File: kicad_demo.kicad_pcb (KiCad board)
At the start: 2 copper layers, 100 x 50 mm, 19 parts, among them P1 pwr, P2 key, Q1 2N3053, Y1 7020 kHz

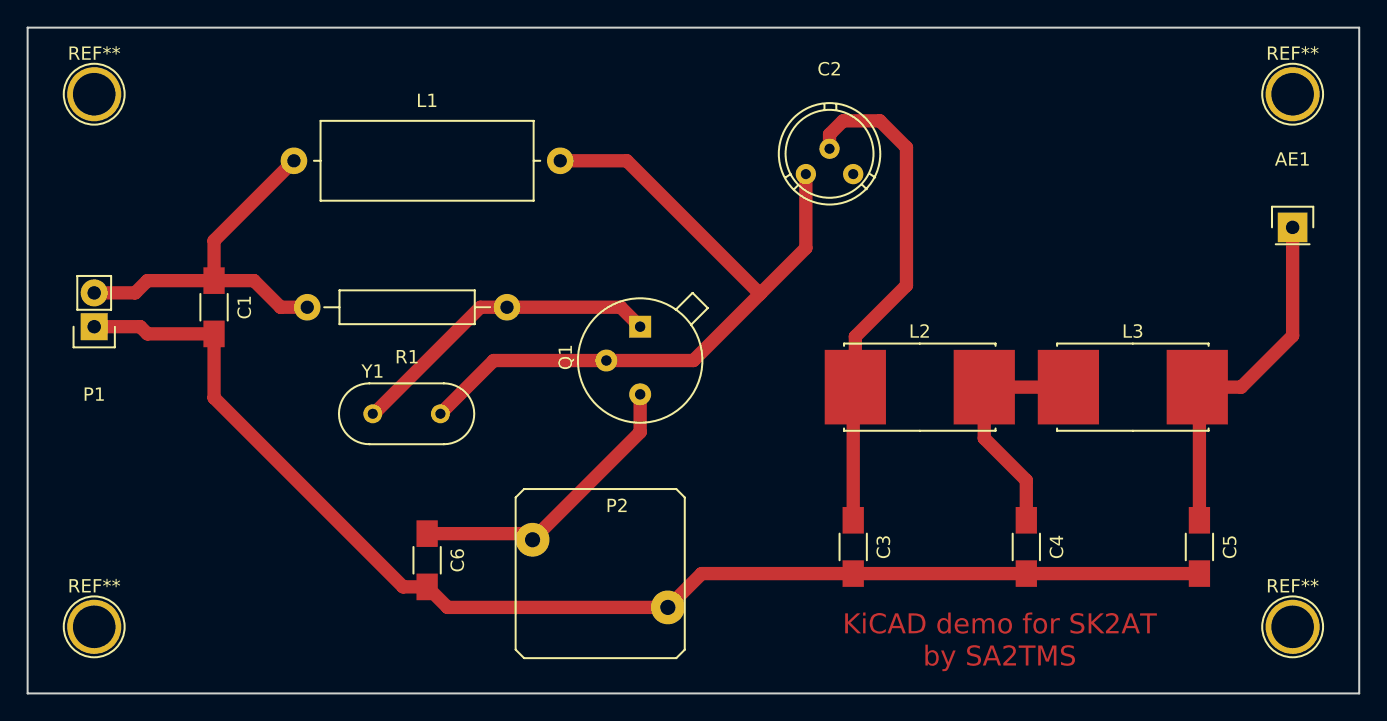
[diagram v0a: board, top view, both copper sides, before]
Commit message: Rough layout
Want to route signal and GND on top to minimize current loop size
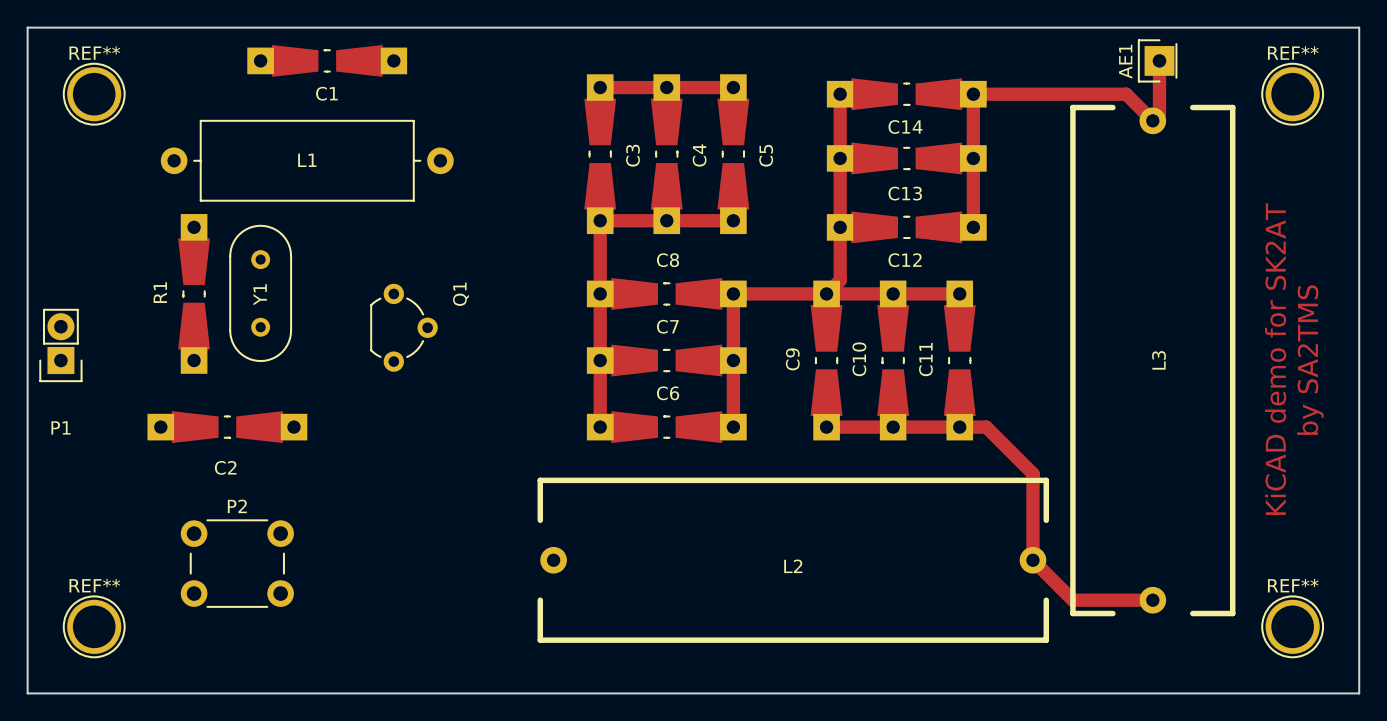
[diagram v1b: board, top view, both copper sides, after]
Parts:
- added C10: 60p, Resistors_Universal:Resistor_SMD+THTuniversal_0805to1206_RM10_HandSoldering, F.Cu at (115.0, 100.0)
- added C11: 5p, Resistors_Universal:Resistor_SMD+THTuniversal_0805to1206_RM10_HandSoldering, F.Cu at (120.0, 100.0)
- added C12: 200p, Resistors_Universal:Resistor_SMD+THTuniversal_0805to1206_RM10_HandSoldering, F.Cu at (116.0, 90.0)
- added C13: 60p, Resistors_Universal:Resistor_SMD+THTuniversal_0805to1206_RM10_HandSoldering, F.Cu at (116.0, 84.8)
- added C14: 7p, Resistors_Universal:Resistor_SMD+THTuniversal_0805to1206_RM10_HandSoldering, F.Cu at (116.0, 80.0)
- added C7: 60p, Resistors_Universal:Resistor_SMD+THTuniversal_0805to1206_RM10_HandSoldering, F.Cu at (98.0, 100.0)
- added C8: 7p, Resistors_Universal:Resistor_SMD+THTuniversal_0805to1206_RM10_HandSoldering, F.Cu at (98.0, 95.0)
- added C9: 800p, Resistors_Universal:Resistor_SMD+THTuniversal_0805to1206_RM10_HandSoldering, F.Cu at (110.0, 100.0)
- AE1: value Antenna -> Ant
- C1: footprint Capacitors_SMD:C_1206_HandSoldering -> Resistors_Universal:Resistor_SMD+THTuniversal_0805to1206_RM10_HandSoldering
- C2: value 1000pF -> 10nF; footprint Potentiometers:Potentiometer_Bourns_3339H_Angular_ScrewUp -> Resistors_Universal:Resistor_SMD+THTuniversal_0805to1206_RM10_HandSoldering
- C3, C5: value 267pF -> 100p; footprint Capacitors_SMD:C_1206_HandSoldering -> Resistors_Universal:Resistor_SMD+THTuniversal_0805to1206_RM10_HandSoldering
- C4: value 865pF -> 100p; footprint Capacitors_SMD:C_1206_HandSoldering -> Resistors_Universal:Resistor_SMD+THTuniversal_0805to1206_RM10_HandSoldering
- C6: value 10nF -> 200p; footprint Capacitors_SMD:C_1206_HandSoldering -> Resistors_Universal:Resistor_SMD+THTuniversal_0805to1206_RM10_HandSoldering
- L2, L3: footprint Inductors:Inductor_Vishay_IHSM-3825 -> PROJECT:1u75_coil
- P2: footprint Buttons_Switches_ThroughHole:SW_PUSH -> Buttons_Switches_ThroughHole:SW_PUSH_6mm
- Q1: value 2N3053 -> BC546; footprint TO_SOT_Packages_THT:TO39EBC -> TO_SOT_Packages_THT:TO-92_Molded_Wide
- R1: footprint Resistors_ThroughHole:Resistor_Horizontal_RM15mm -> Resistors_Universal:Resistor_SMD+THTuniversal_0805to1206_RM10_HandSoldering
- moved C2 47.4 mm to (65.0, 105.0), turned to 180 degrees
- moved C5 45.8 mm to (103.0, 84.5)
- moved C4 40.0 mm to (98.0, 84.5)
- moved C3 35.1 mm to (93.0, 84.5)
- moved P2 30.6 mm to (62.5, 113.0)
- moved R1 23.5 mm to (62.5, 95.0), turned to 90 degrees
- moved C6 20.6 mm to (98.0, 105.0), turned to 0 degrees
- moved C1 20.4 mm to (72.5, 77.5), turned to 0 degrees
- moved Q1 18.7 mm to (77.5, 95.0)
- moved L2 16.1 mm to (107.5, 115.0)
- moved AE1 16.0 mm to (135.0, 77.5), turned to 90 degrees
- moved Y1 10.6 mm to (67.5, 97.5), turned to 90 degrees
- moved L1 9.00 mm to (71.0, 85.0)
- moved P1 3.56 mm to (52.5, 100.0)
- moved L3 2.50 mm to (134.5, 100.0), turned to 90 degrees
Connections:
- C2 pad 2: Net-(C2-Pad2) -> GND
- C3 pad 1: Net-(C2-Pad2) -> Net-(C3-Pad1)
- C3 pad 2: GND -> Net-(C3-Pad2)
- C4 pad 1: Net-(C4-Pad1) -> Net-(C3-Pad1)
- C4 pad 2: GND -> Net-(C3-Pad2)
- C5 pad 1: Net-(AE1-Pad1) -> Net-(C3-Pad1)
- C5 pad 2: GND -> Net-(C3-Pad2)
- C6 pad 1: Net-(C6-Pad1) -> Net-(C3-Pad2)
- L1 pad 2: Net-(C2-Pad1) -> Net-(C3-Pad1)
- L2 pad 1: Net-(C2-Pad2) -> Net-(C3-Pad2)
- L2 pad 2: Net-(C4-Pad1) -> Net-(C10-Pad1)
- L3 pad 1: Net-(C4-Pad1) -> Net-(C10-Pad1)
- P2 pad 1: Net-(C6-Pad1) -> Net-(C2-Pad1)
- Q1 pad 1: Net-(Q1-Pad1) -> Net-(C3-Pad1)
- Q1 pad 2: Net-(C2-Pad1) -> Net-(Q1-Pad2)
- Q1 pad 3: Net-(C6-Pad1) -> Net-(C2-Pad1)
- R1 pad 1: Net-(Q1-Pad1) -> Net-(Q1-Pad2)
- Y1 pad 1: Net-(Q1-Pad1) -> Net-(Q1-Pad2)
- Y1 pad 2: Net-(C2-Pad1) -> Net-(C3-Pad1)
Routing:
- net Net-(C2-Pad1): track 57.3 -> 0.00 mm
- net Net-(C10-Pad1): track 0.00 -> 41.5 mm
- net Net-(C3-Pad2): track 0.00 -> 41.0 mm
- net Net-(C2-Pad2): track 37.8 -> 0.00 mm
- net GND: track 95.6 -> 65.7 mm
- net +9V: track 28.7 -> 0.00 mm
- net Net-(Q1-Pad1): track 24.0 -> 0.00 mm
- net Net-(C6-Pad1): track 22.4 -> 0.00 mm
- net Net-(C3-Pad1): track 0.00 -> 17.8 mm
- net Net-(C4-Pad1): track 17.6 -> 0.00 mm
- net Net-(AE1-Pad1): track 27.0 -> 36.8 mm
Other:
- board text added: "9V battery"

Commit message: Mostly done
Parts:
- moved P1 7.16 mm to (55.5, 93.5), turned to 0 degrees
- moved P2 6.52 mm to (69.0, 113.5)
- moved Q1 4.72 mm to (82.0, 96.4)
- moved L1 4.61 mm to (75.5, 86.0)
- moved C1 3.61 mm to (75.5, 79.5)
- moved Y1 2.72 mm to (70.0, 98.6)
- moved R1 1.50 mm to (61.0, 95.0)
- moved L2 1.50 mm to (106.0, 115.0)
- moved L3 1.50 mm to (133.0, 100.0)
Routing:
- net GND: track 65.7 -> 185.6 mm
- net Net-(C3-Pad1): track 17.8 -> 54.5 mm
- net Net-(C2-Pad1): track 0.00 -> 31.5 mm
- net +9V: track 0.00 -> 29.1 mm
- net Net-(Q1-Pad2): track 0.00 -> 26.9 mm
- net Net-(C3-Pad2): track 41.0 -> 54.3 mm
- net Net-(AE1-Pad1): track 36.8 -> 35.9 mm
- net Net-(C10-Pad1): track 41.5 -> 40.8 mm

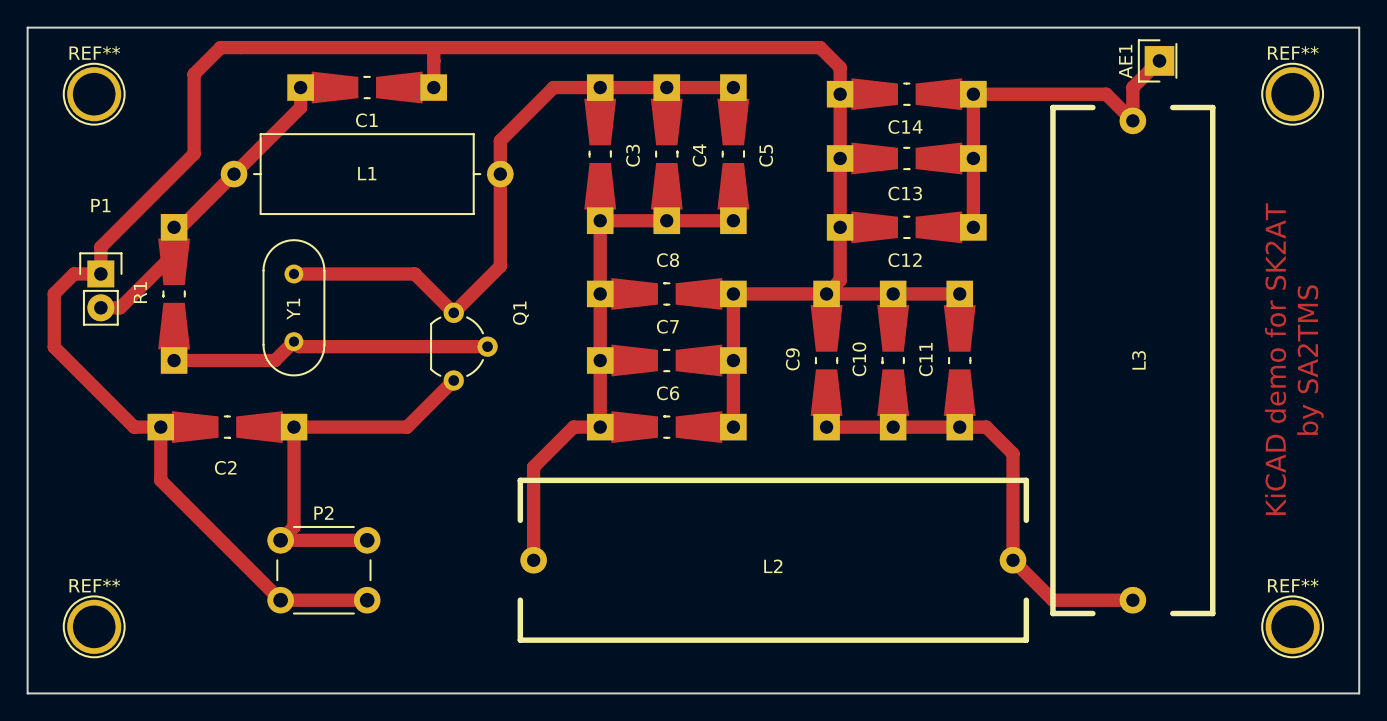
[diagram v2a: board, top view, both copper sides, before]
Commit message: Fiddle with layout, add more transistors
Vertically centered L2 wrt L3, to reduce coupling.
Increased distance between signal and GND trace.
Added two copies of Q1 next to it, in case more power is wanted.
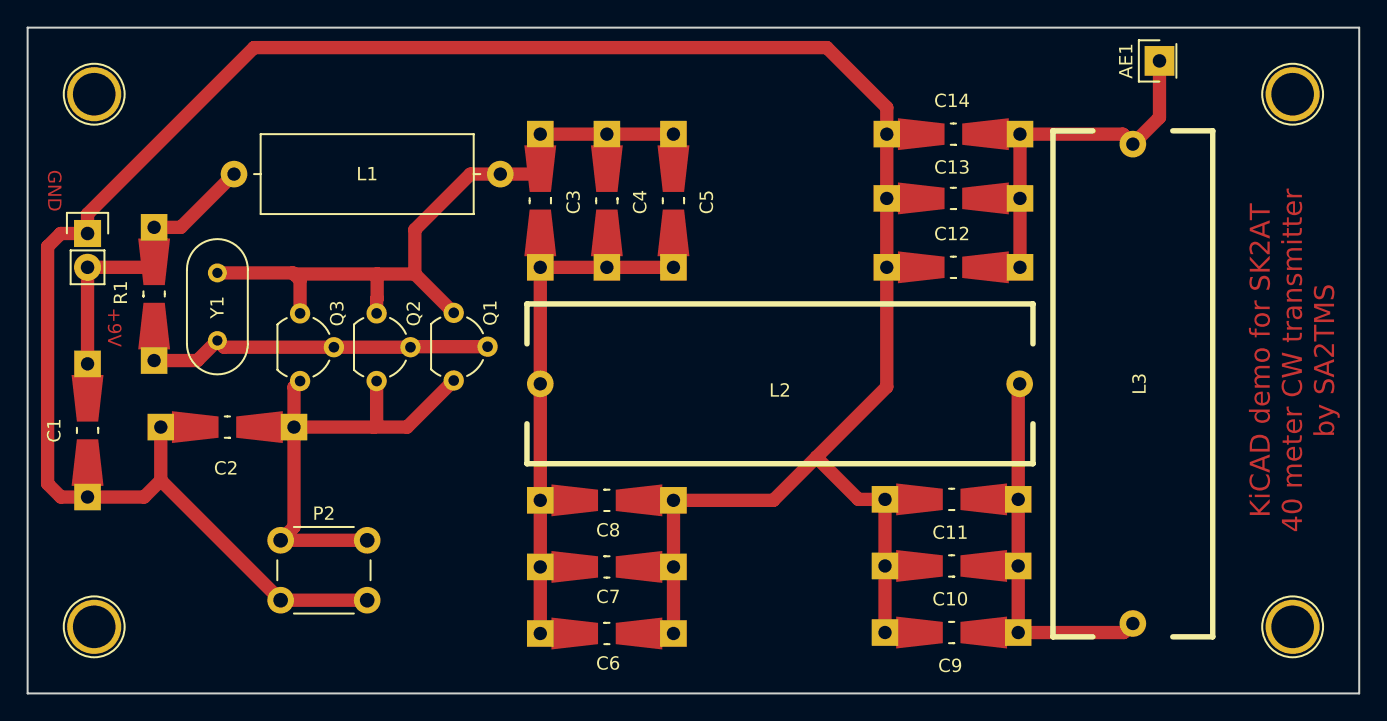
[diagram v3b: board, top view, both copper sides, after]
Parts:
- added Q2: BC546, TO_SOT_Packages_THT:TO-92_Molded_Wide, F.Cu at (76.2, 96.5)
- added Q3: BC546, TO_SOT_Packages_THT:TO-92_Molded_Wide, F.Cu at (70.5, 96.5)
- AE1: value Ant -> Antenna
- moved C1 33.2 mm to (54.5, 105.2), turned to 270 degrees
- moved C9 22.5 mm to (119.4, 120.4), turned to 180 degrees
- moved C6 16.1 mm to (93.5, 120.5)
- moved C7 16.1 mm to (93.5, 115.5)
- moved C8 16.1 mm to (93.5, 110.5)
- moved C10 16.0 mm to (119.4, 115.4), turned to 180 degrees
- moved L2 13.3 mm to (106.5, 101.8)
- moved C11 10.4 mm to (119.4, 110.4), turned to 180 degrees
- moved Y1 5.75 mm to (64.2, 98.5)
- moved C3 5.70 mm to (88.5, 88.0)
- moved C4 5.70 mm to (93.5, 88.0)
- moved C5 5.70 mm to (98.5, 88.0)
- moved C12 4.61 mm to (119.5, 93.0)
- moved C13 4.61 mm to (119.5, 87.8)
- moved C14 4.61 mm to (119.5, 83.0)
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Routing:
- net GND: track 185.6 -> 217.9 mm
- net Net-(C2-Pad1): track 31.5 -> 38.6 mm
- net Net-(C10-Pad1): track 40.8 -> 35.4 mm
- net +9V: track 29.1 -> 25.3 mm
- net Net-(C3-Pad1): track 54.5 -> 57.5 mm
- net Net-(AE1-Pad1): track 35.9 -> 33.6 mm
- net Net-(Q1-Pad2): track 26.9 -> 28.5 mm
- net Net-(C3-Pad2): track 54.3 -> 53.0 mm
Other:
- board text added: "+9V"
- board text added: "GND"
- board text added: "KiCAD demo for SK2AT 40 meter CW transmitter by SA2TMS"
- board text removed: "9V battery"
- board text removed: "KiCAD demo for SK2AT by SA2TMS"
